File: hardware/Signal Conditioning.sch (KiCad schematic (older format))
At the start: 22 parts, among them U2 LM324, U3 LM324

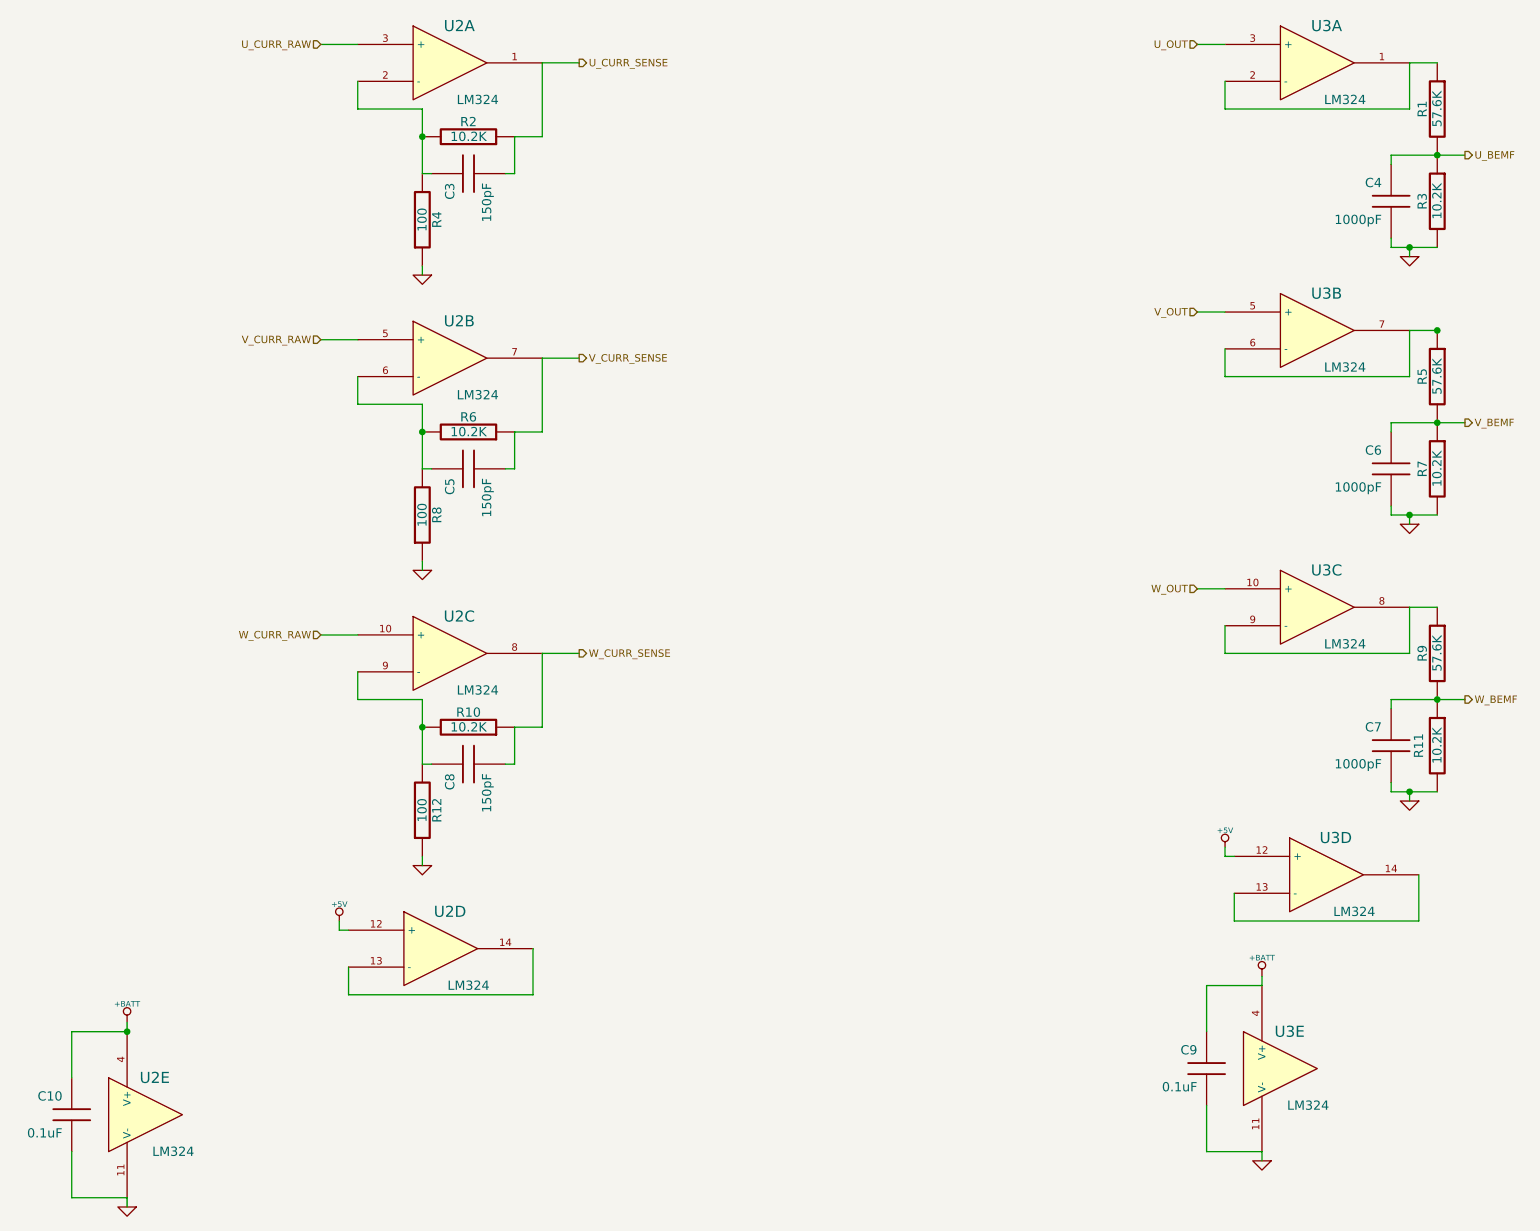
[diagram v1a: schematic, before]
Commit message: Updated the Part number and footprints for most components
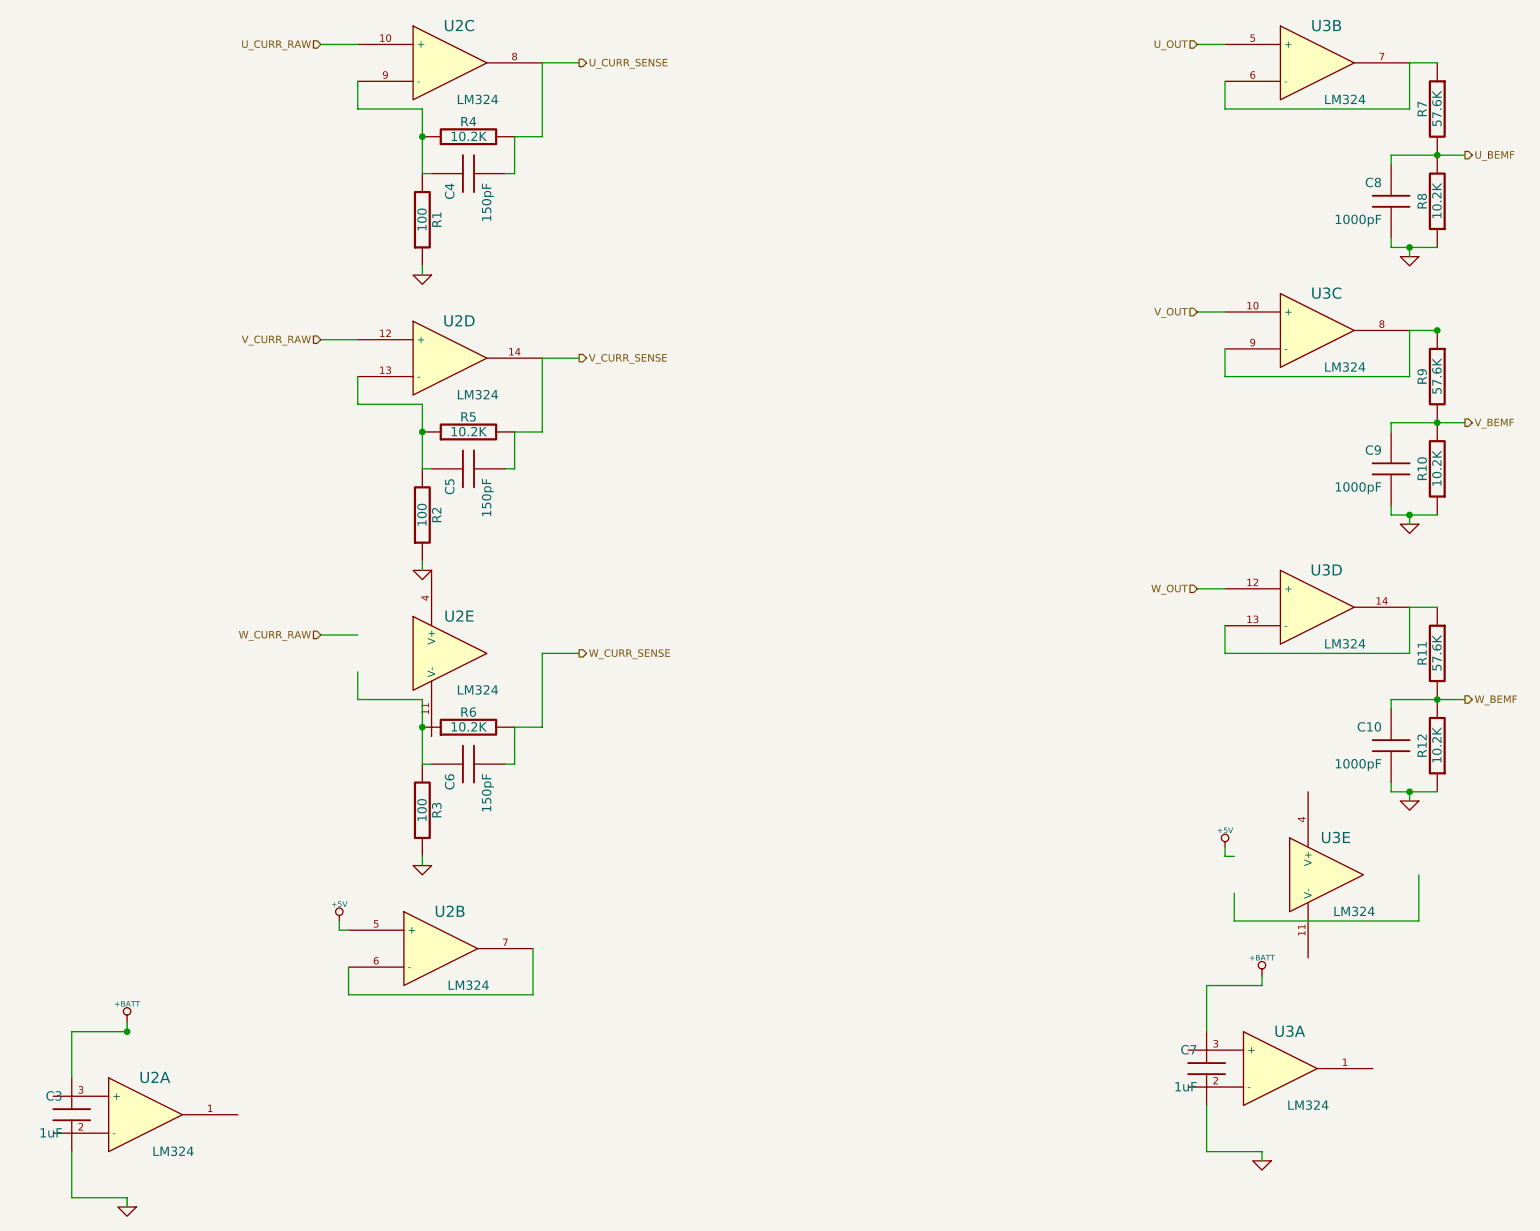
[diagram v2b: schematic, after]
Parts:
- removed C6: 1000pF, 0805, symbol C
- removed R2, R3, R7: 10.2K, 0805, symbol R
- removed unit 2 of U2
- added C3: 1uF, 0805, symbol C
- added R12, R4, R8: 10.2K, 0805, symbol R
- added unit 4 of U2
- C10, C9: value 0.1uF -> 1000pF; Digikey P/N 1276-1828-1-ND -> 1276-1020-1-ND; Mfg P/N CL21C151JBANNNC -> CL21B102KBANNNC
- C7: value 1000pF -> 1uF; Digikey P/N 1276-1828-1-ND -> 1276-3010-1-ND; Mfg P/N CL21C151JBANNNC -> CL21F105ZBFNNNE
- C8: renamed from C4; Digikey P/N 1276-1828-1-ND -> 1276-1020-1-ND; Mfg P/N CL21C151JBANNNC -> CL21B102KBANNNC
- R10, R6: Digikey P/N P1.02BTCT-ND -> P10.2KCCT-ND; Mfg P/N ERJ-6ENF1024V -> ERJ-6ENF1022V; Mouser P/N 667-ERJ-6ENF1024V -> 667-ERJ-6ENF1022V
- R11: value 10.2K -> 57.6K; Digikey P/N P1.02BTCT-ND -> P56.2KCCT-ND; Mfg P/N ERJ-6ENF1024V -> ERJ-6ENF5622V; Mouser P/N 667-ERJ-6ENF1024V -> 667-ERJ-6ENF5622V
- R5: value 57.6K -> 10.2K; Digikey P/N P1.02BTCT-ND -> P10.2KCCT-ND; Mfg P/N ERJ-6ENF1024V -> ERJ-6ENF1022V; Mouser P/N 667-ERJ-6ENF1024V -> 667-ERJ-6ENF1022V
- R7: renamed from R1; Digikey P/N P1.02BTCT-ND -> P56.2KCCT-ND; Mfg P/N ERJ-6ENF1024V -> ERJ-6ENF5622V; Mouser P/N 667-ERJ-6ENF1024V -> 667-ERJ-6ENF5622V
- R9: Digikey P/N P1.02BTCT-ND -> P56.2KCCT-ND; Mfg P/N ERJ-6ENF1024V -> ERJ-6ENF5622V; Mouser P/N 667-ERJ-6ENF1024V -> 667-ERJ-6ENF5622V
- U2, U3: footprint (none) -> SOIC-14; Digikey P/N (none) -> 296-9540-1-ND; Mfg P/N (none) -> LM324ADR; Mouser P/N (none) -> 595-LM324ADR
- renumbered C3 to C4, C8 to C6, R4 to R1, R8 to R2, R12 to R3
